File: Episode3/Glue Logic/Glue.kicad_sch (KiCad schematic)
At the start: 17 parts, among them U11 ATF22V10, U12 ATF750C, U7 ATF22V10C, U8 ATF22V10, U9 ATF750C, X1 1MHz

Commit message: Tied up a few loose ends in the PLD page.
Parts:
- X1: value 1MHz -> 20MHz
- renumbered R8 to R6, R6 to R8, U12 to U10

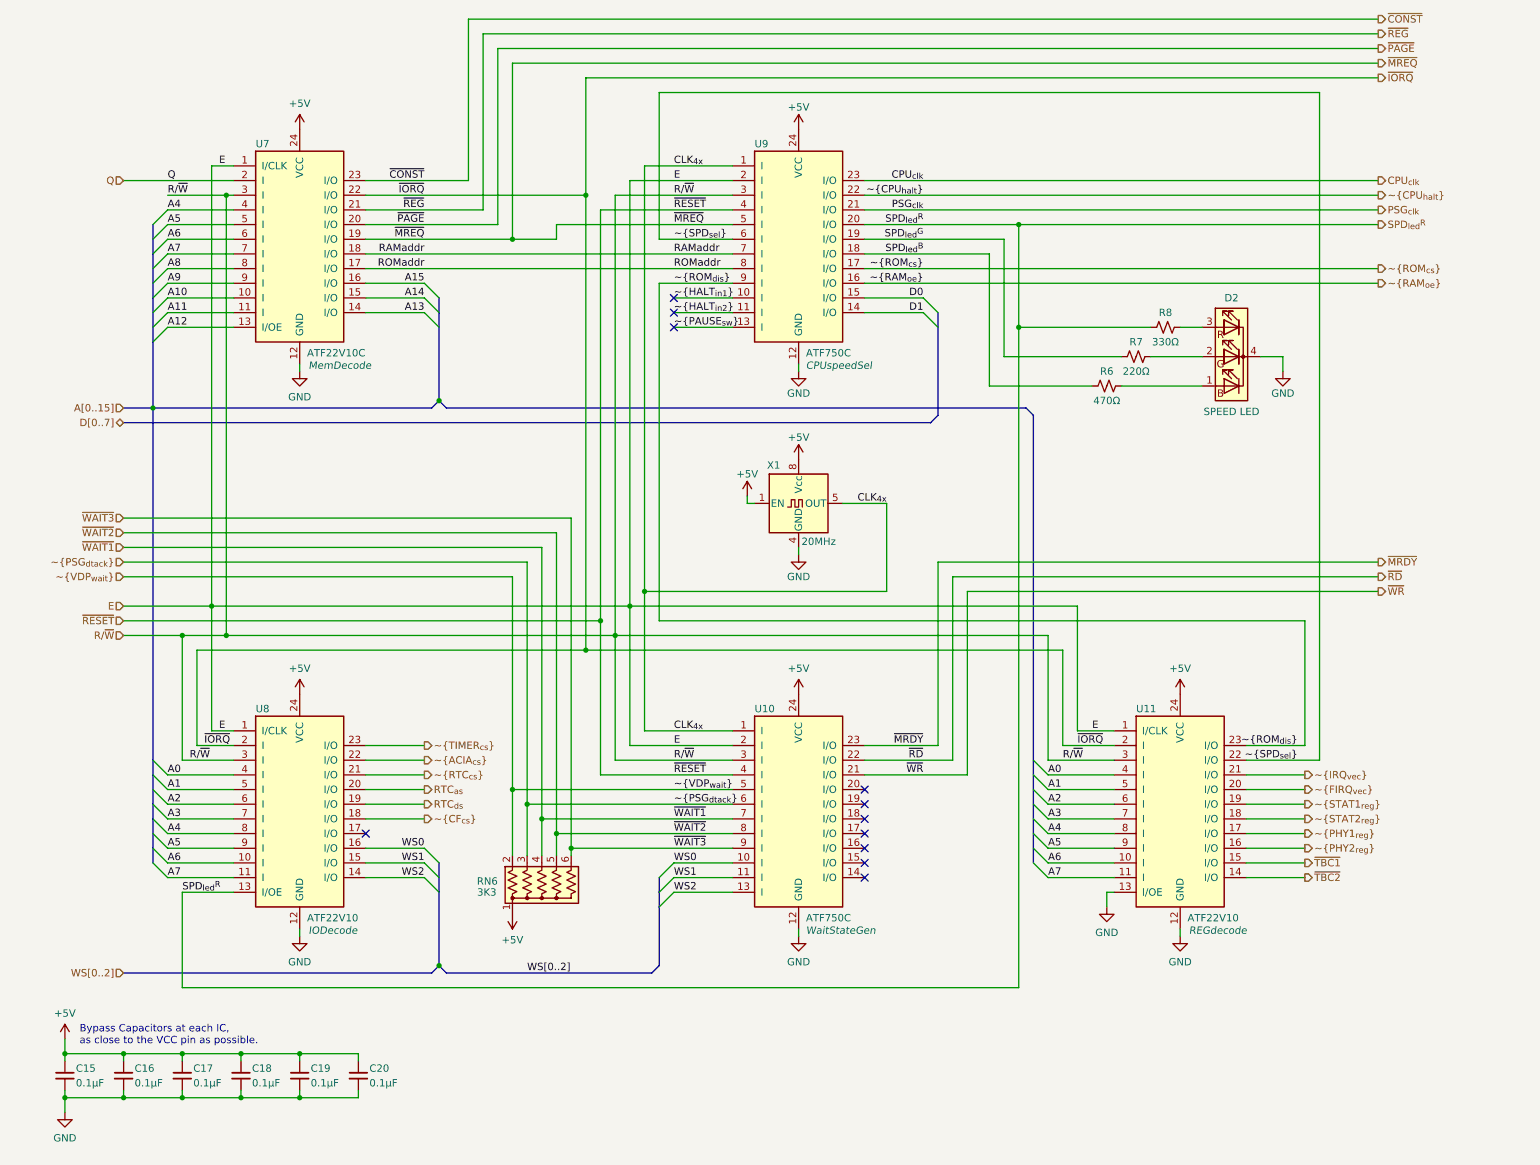
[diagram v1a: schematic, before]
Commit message: Corrected OE error
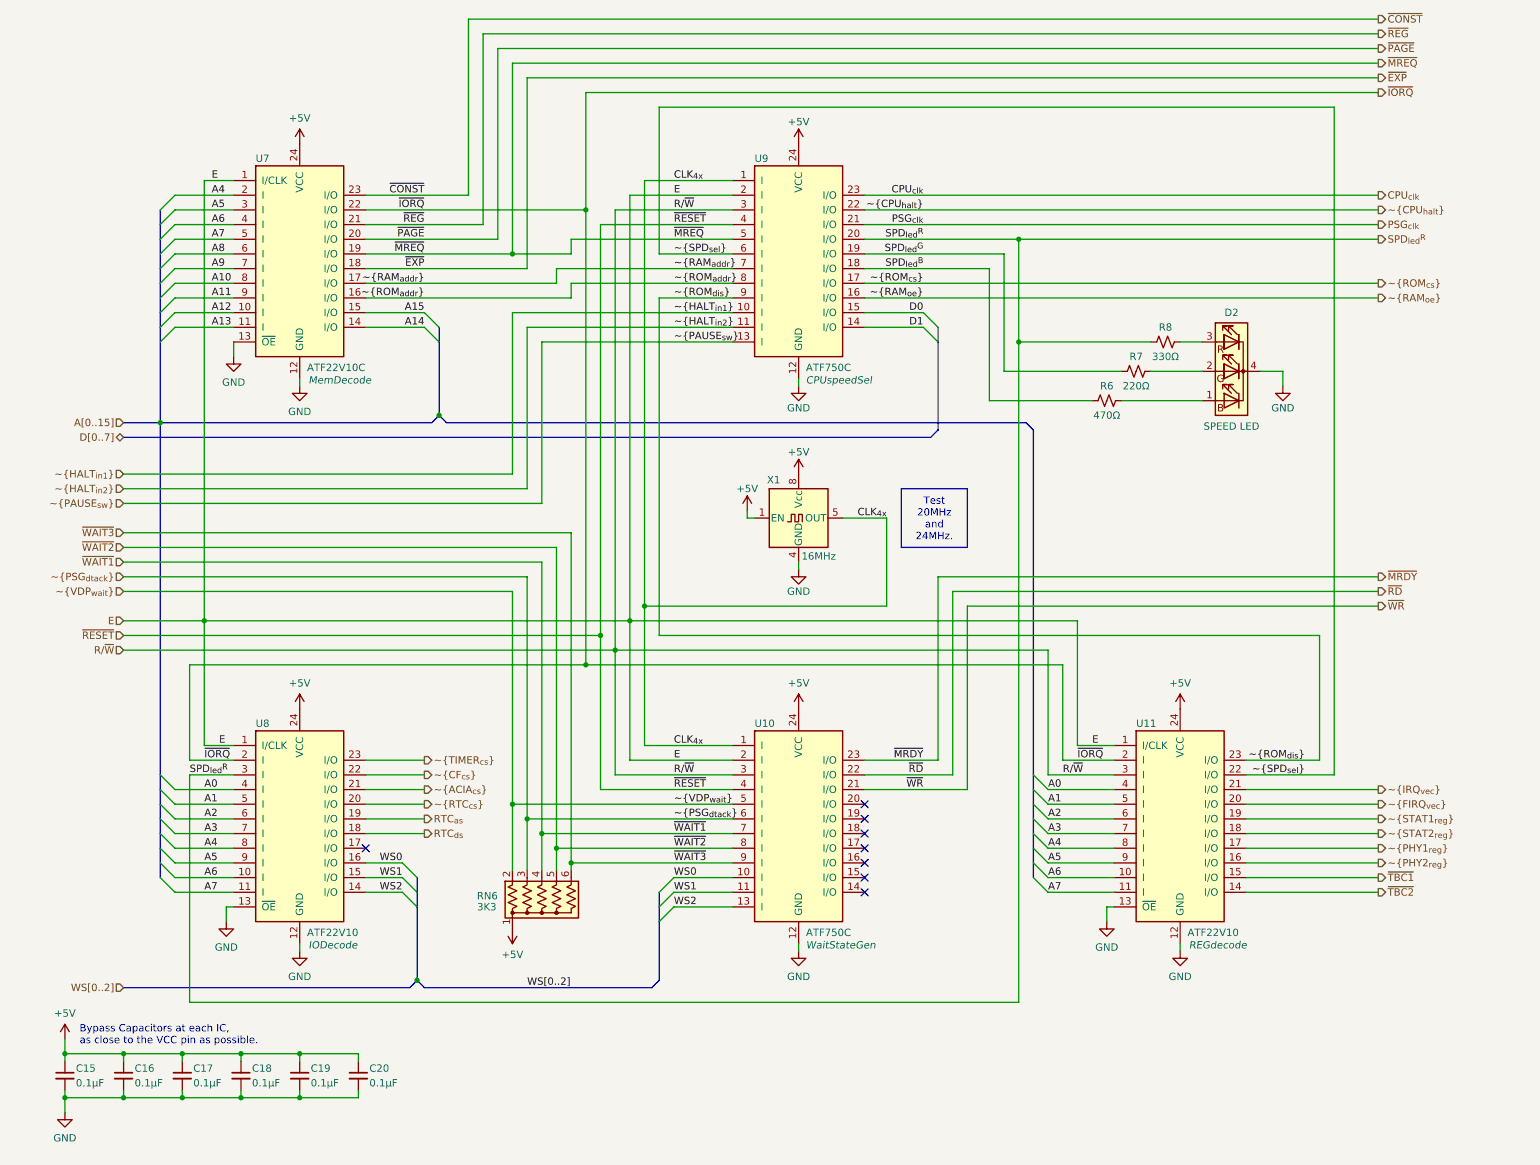
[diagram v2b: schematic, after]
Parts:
- X1: value 20MHz -> 16MHz
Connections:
- net Q is gone; now on net A4: U7.2 (I)
- net A10: now also U7.8 (I); no longer U7.10 (I)
- net A11: now also U7.9 (I); no longer U7.11 (I)
- net A12: now also U7.10 (I); no longer U7.13 (I/OE)
- net A13: now also U7.11 (I); no longer U7.14 (I/O)
- net A14: now also U7.14 (I/O); no longer U7.15 (I/O)
- net A15: now also U7.15 (I/O); no longer U7.16 (I/O)
- net A4: no longer U7.4 (I)
- net A5: now also U7.3 (I); no longer U7.5 (I)
- net A6: now also U7.4 (I); no longer U7.6 (I)
- net A7: now also U7.5 (I); no longer U7.7 (I)
- net A8: now also U7.6 (I); no longer U7.8 (I)
- net A9: now also U7.7 (I); no longer U7.9 (I)
- net GND: now also U7.13 (~{OE}), U8.13 (~{OE})
- net RTC_{as}: now also U8.19 (I/O); no longer U8.20 (I/O)
- net RTC_{ds}: now also U8.18 (I/O); no longer U8.19 (I/O)
- net R/~{W}: no longer U7.3 (I), U8.3 (I)
- net SPD_{led}^{R}: now also U8.3 (I); no longer U8.13 (I/OE)
- net ~{ACIA_{cs}}: now also U8.21 (I/O); no longer U8.22 (I/O)
- net ~{CF_{cs}}: now also U8.22 (I/O); no longer U8.18 (I/O)
- net ~{RTC_{cs}}: now also U8.20 (I/O); no longer U8.21 (I/O)
- net RAMaddr renamed ~{EXP}
- net ~{EXP}: no longer U9.7 (I)
- net ROMaddr renamed ~{RAM_{addr}}
- net ~{RAM_{addr}}: now also U9.7 (I); no longer U9.8 (I)
- new net ~{ROM_{addr}}: U7.16 (I/O), U9.8 (I)
- no-connect marks 11 -> 8
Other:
- moved on the sheet: D2, R6, R7, R8, RN6, U10, U11, U7, U8, U9, X1

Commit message: Major updates to PLDs
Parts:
- added R10, R13, R14, R15, R16, R17, R18, R9: 3K3Ω, symbol Device:R_Small_US
- RN6: value 3K3 -> 3K3Ω
- U10: Position (none) -> BB-Right
- U11: footprint Package_DIP:DIP-24_W7.62mm_Socket -> Package_DIP:DIP-24_W7.62mm_Socket_LongPads; Position (none) -> BB-C/Left
- U7: Position (none) -> BB-Left
- U8: footprint Package_DIP:DIP-24_W7.62mm_Socket -> Package_DIP:DIP-24_W7.62mm_Socket_LongPads; Position (none) -> BB-C/Right
- U9: Position (none) -> BB-Top
- X1: value 16MHz -> 12MHz
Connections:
- net PSG_{clk} is gone; now on net SPD_{led}^{R}: U9.21 (I/O)
- net ~{EXP} is gone; now on net ~{ROM_{addr}}: U7.18 (I/O)
- net ~{HALT_{in1}} is gone; now on net ~{ROM_{addr}}: U9.10 (I)
- net ~{HALT_{in2}} is gone; now on net ~{RAM_{addr}}: U9.11 (I)
- net ~{TBC1} is gone; now on net ~{RD}: U11.15 (I/O)
- net ~{TBC2} is gone; now on net ~{WR}: U11.14 (I/O)
- net +5V: now also R13.1, R15.1, R16.1, R17.1, R18.1
- net A0: now also U8.2 (I); no longer U8.4 (I)
- net A1: now also U8.3 (I); no longer U8.5 (I)
- net A14: now also U7.13 (I/OE); no longer U7.14 (I/O)
- net A15: now also U7.14 (I/O); no longer U7.15 (I/O)
- net A2: now also U8.4 (I); no longer U8.6 (I)
- net A3: now also U8.5 (I); no longer U8.7 (I)
- net A4: now also U8.6 (I); no longer U8.8 (I)
- net A5: now also U8.7 (I); no longer U8.9 (I)
- net A6: now also U8.8 (I); no longer U8.10 (I)
- net A7: now also U8.9 (I); no longer U8.11 (I)
- net CLK_{4x}: no longer U10.1 (I)
- net CPU_{clk}: now also U10.1 (I)
- net E: no longer U8.1 (I/CLK)
- net GND: now also U9.13 (I), R10.1, R14.1, R9.1; no longer U7.13 (~{OE}), U8.13 (~{OE})
- net SPD_{led}^{B}: now also U9.19 (I/O); no longer U9.18 (I/O)
- net SPD_{led}^{G}: now also U8.11 (I), U9.20 (I/O); no longer U9.19 (I/O)
- net SPD_{led}^{R}: now also U8.10 (I); no longer U8.3 (I), U9.20 (I/O)
- net WS0: now also R14.2
- net WS1: now also R9.2
- net WS2: now also R10.2; no longer U8.14 (I/O)
- net ~{IORQ}: now also U8.1 (I/CLK); no longer U8.2 (I)
- net ~{PAUSE_{sw}}: now also U9.9 (I), R17.2; no longer U9.13 (I)
- net ~{RAM_{addr}}: now also R16.2; no longer U9.7 (I)
- net ~{RD}: no longer U10.22 (I/O)
- net ~{ROM_{addr}}: now also R15.2; no longer U7.16 (I/O), U9.8 (I)
- net ~{ROM_{dis}}: now also U9.6 (I); no longer U9.9 (I)
- net ~{SPD_{sel}}: now also U9.7 (I); no longer U9.6 (I)
- net ~{WR}: no longer U10.21 (I/O)
- net ~{USB_{cs}}: now reaches U8.17 (I/O)
- new net: R13.2, U8.13 (I/OE), U8.14 (I/O)
- new net ~{HALT_{in}}: R18.2, U9.8 (I)
- new net ~{RAM_{cs}}*: U9.18 (I/O)
- no-connect marks 8 -> 11
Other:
- moved on the sheet: C15, C16, C17, C18, C19, C20, D2, R6, R7, R8, RN6, U10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

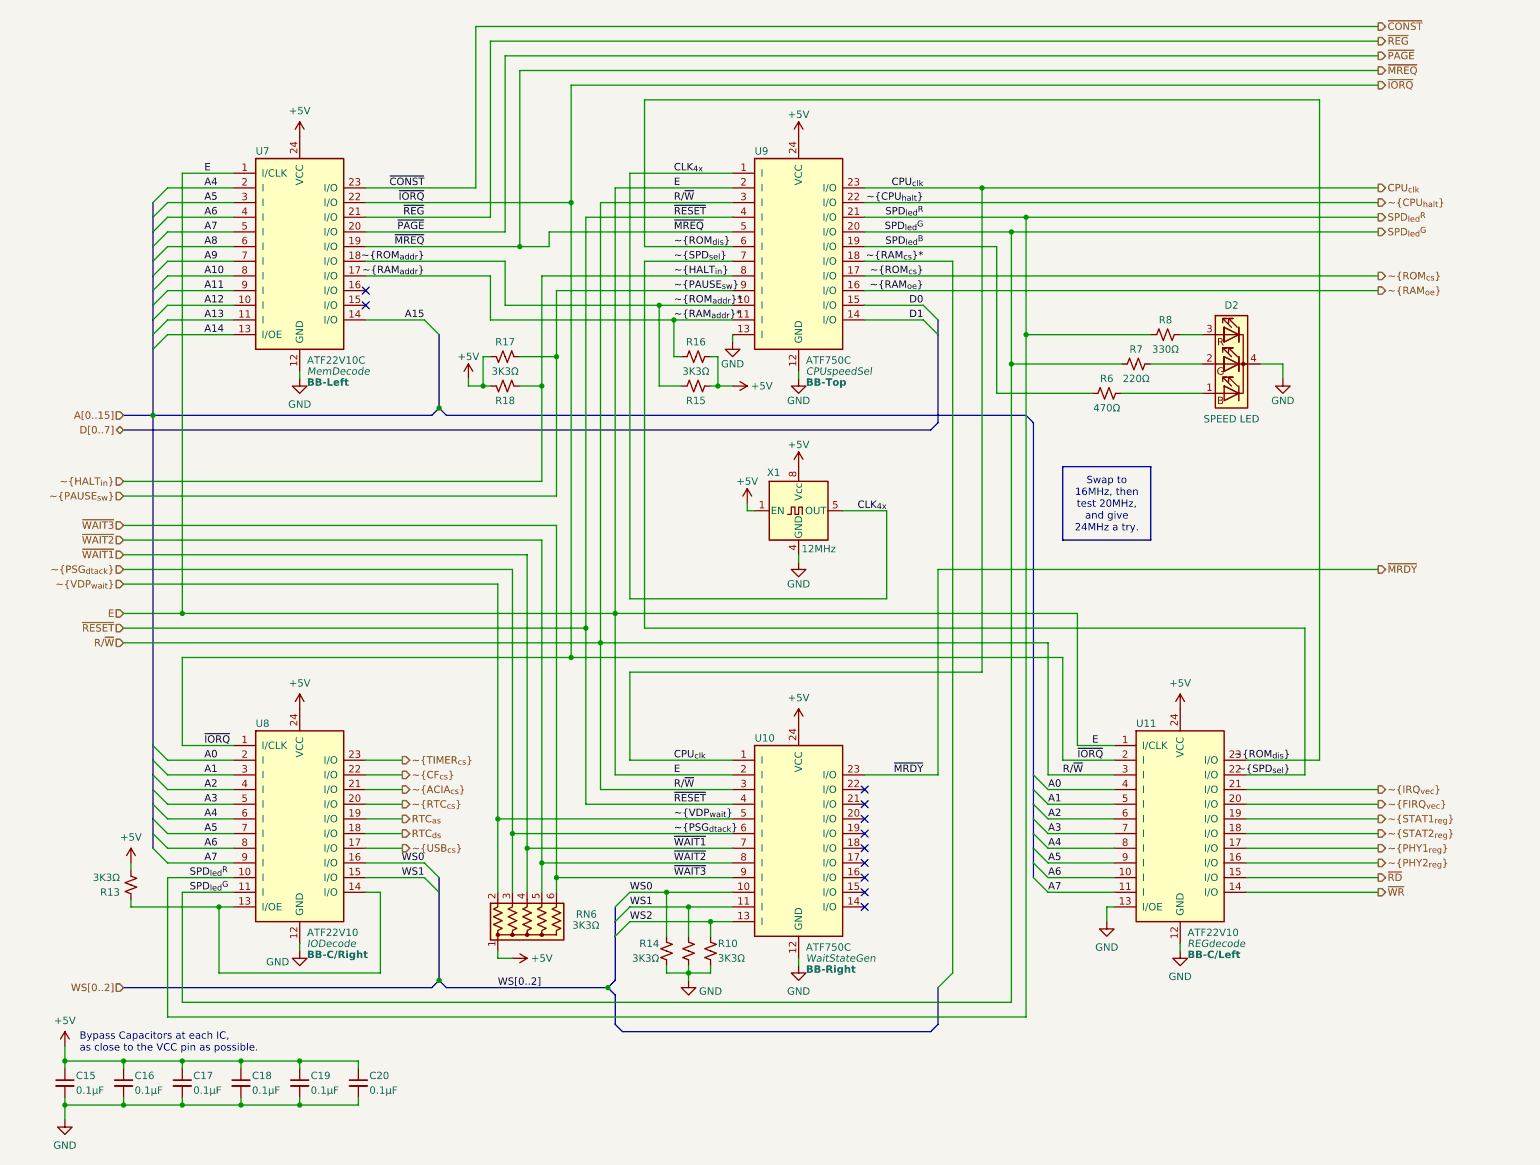
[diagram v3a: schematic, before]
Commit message: Reduced PLDs from 5 to 4, and optimized macrocells to the maximum
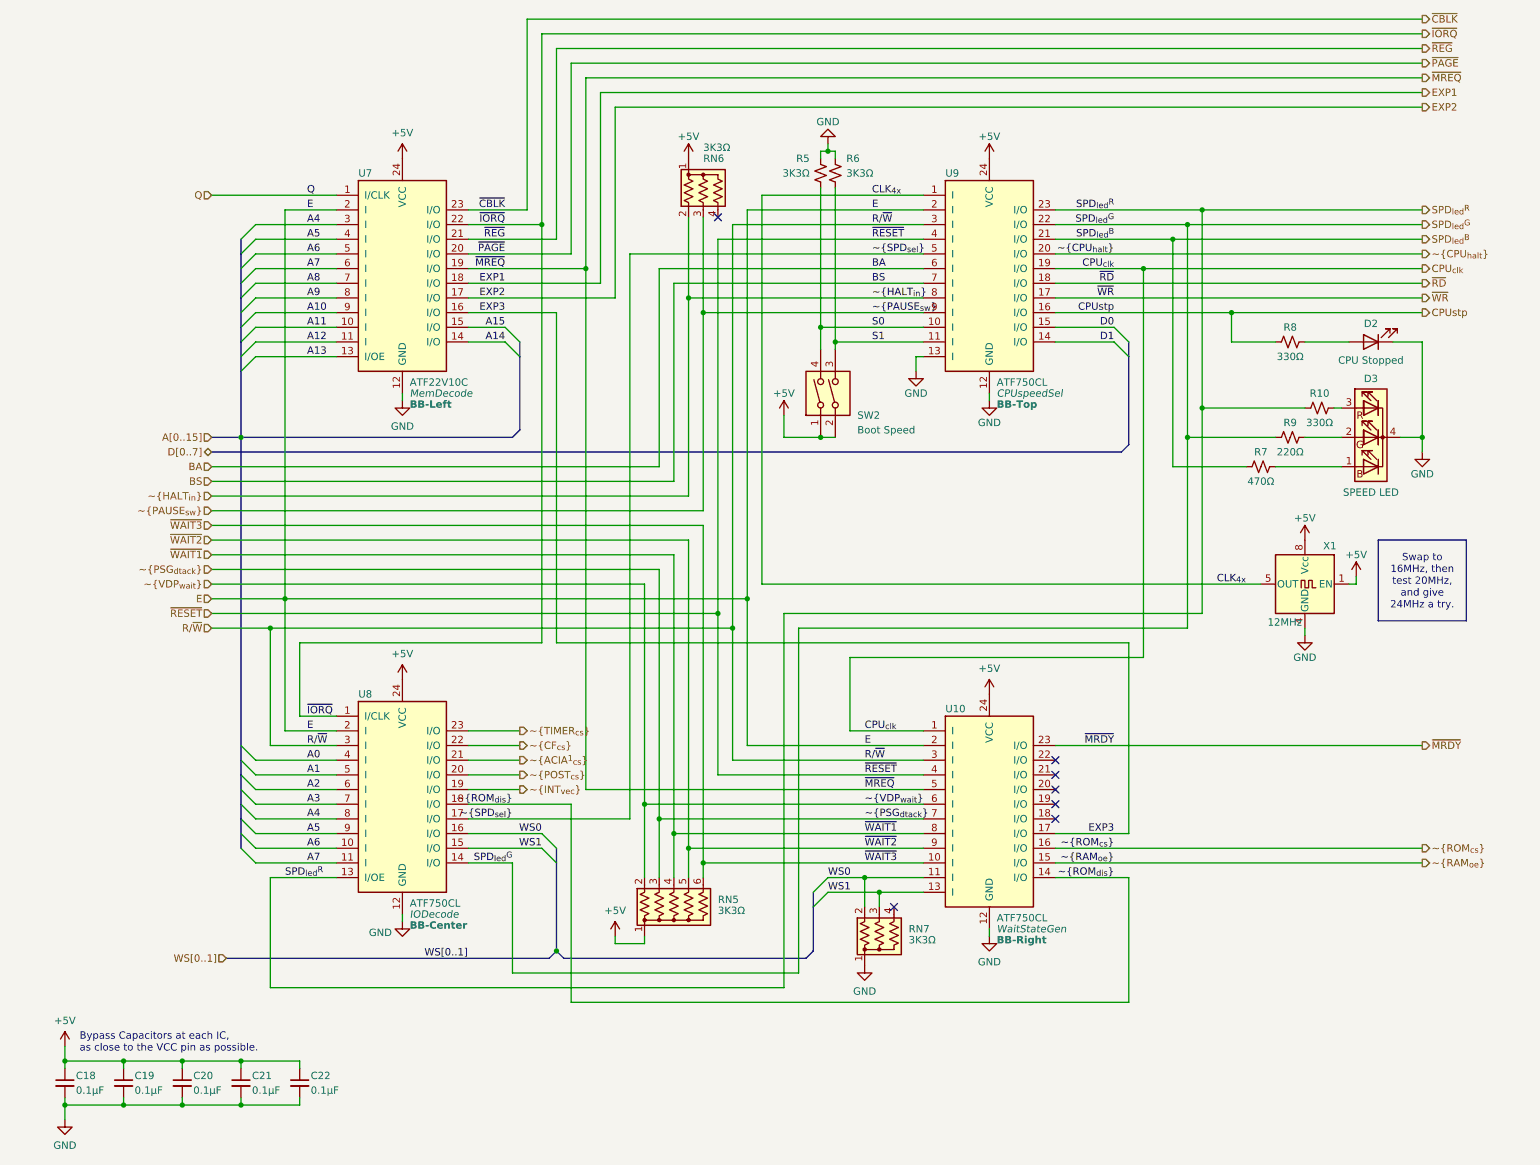
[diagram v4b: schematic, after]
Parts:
- removed C20: 0.1µF, symbol Device:C_Small
- removed R10, R13, R14, R15, R16, R17, R18, R9: 3K3Ω, symbol Device:R_Small_US
- removed U11: ATF22V10, Package_DIP:DIP-24_W7.62mm_Socket_LongPads, symbol MicroHobbyist:ATF22V10C
- added D2: CPU Stopped, symbol Device:LED
- added R5, R6: 3K3Ω, symbol Device:R_Small_US
- added R8: 330Ω, symbol Device:R_Small_US
- added RN6, RN7: 3K3Ω, Resistor_THT:R_Array_SIP4, symbol Device:R_Network03_US
- added SW2: Boot Speed, symbol Switch:SW_DIP_x02
- U10, U9: value ATF750C -> ATF750CL
- U8: value ATF22V10 -> ATF750CL; Position BB-C/Right -> BB-Center
- renumbered C15 to C18, C16 to C19, C17 to C20, C18 to C21, C19 to C22, D2 to D3, R8 to R10, R6 to R7, R7 to R9, RN6 to RN5
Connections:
- net RTC_{ds} is gone; now on net ~{ROM_{dis}}: U8.18 (I/O)
- net WS2 is gone; now on net WS1: U10.13 (I)
- net ~{RAM_{cs}}* is gone; now on net ~{RD}: U9.18 (I/O)
- net ~{USB_{cs}} is gone; now on net ~{SPD_{sel}}: U8.17 (I/O)
- net +5V: now also RN6.1 (common), SW2.1, SW2.2
- net A0: now also U8.4 (I); no longer U8.2 (I)
- net A1: now also U8.5 (I); no longer U8.3 (I)
- net A10: now also U7.9 (I); no longer U7.8 (I)
- net A11: now also U7.10 (I); no longer U7.9 (I)
- net A12: now also U7.11 (I); no longer U7.10 (I)
- net A13: now also U7.13 (I/OE); no longer U7.11 (I)
- net A14: now also U7.14 (I/O); no longer U7.13 (I/OE)
- net A15: now also U7.15 (I/O); no longer U7.14 (I/O)
- net A2: now also U8.6 (I); no longer U8.4 (I)
- net A3: now also U8.7 (I); no longer U8.5 (I)
- net A4: now also U7.3 (I), U8.8 (I); no longer U7.2 (I), U8.6 (I)
- net A5: now also U7.4 (I), U8.9 (I); no longer U7.3 (I), U8.7 (I)
- net A6: now also U7.5 (I), U8.10 (I); no longer U7.4 (I), U8.8 (I)
- net A7: now also U7.6 (I), U8.11 (I); no longer U7.5 (I), U8.9 (I)
- net A8: now also U7.7 (I); no longer U7.6 (I)
- net A9: now also U7.8 (I); no longer U7.7 (I)
- net CPU_{clk}: now also U9.19 (I/O); no longer U9.23 (I/O)
- net E: now also U7.2 (I), U8.2 (I); no longer U7.1 (I/CLK)
- net GND: now also D2.1 (K), R5.2, R6.2, RN7.1 (common)
- net R/~{W}: now also U8.3 (I)
- net SPD_{led}^{B}: now also U9.21 (I/O); no longer U9.19 (I/O)
- net SPD_{led}^{G}: now also U8.14 (I/O), U9.22 (I/O); no longer U8.11 (I), U9.20 (I/O)
- net SPD_{led}^{R}: now also U8.13 (I/OE), U9.23 (I/O); no longer U8.10 (I), U9.21 (I/O)
- net WS0: now also U10.11 (I), RN7.2 (R1); no longer U10.10 (I)
- net WS1: now also RN7.3 (R2); no longer U10.11 (I)
- net ~{CPU_{halt}}: now also U9.20 (I/O); no longer U9.22 (I/O)
- net ~{HALT_{in}}: now also RN6.2 (R1)
- net ~{MREQ}: now also U10.5 (I); no longer U9.5 (I)
- net ~{PAUSE_{sw}}: now also RN6.3 (R2)
- net ~{PSG_{dtack}}: now also U10.7 (I); no longer U10.6 (I)
- net ~{RAM_{oe}}: now also U10.15 (I/O); no longer U9.16 (I/O)
- net ~{ROM_{cs}}: now also U10.16 (I/O); no longer U9.17 (I/O)
- net ~{ROM_{dis}}: now also U10.14 (I/O); no longer U9.6 (I)
- net ~{SPD_{sel}}: now also U9.5 (I); no longer U9.7 (I)
- net ~{VDP_{wait}}: now also U10.6 (I); no longer U10.5 (I)
- net ~{WAIT1}: now also U10.8 (I); no longer U10.7 (I)
- net ~{WAIT2}: now also U10.9 (I); no longer U10.8 (I)
- net ~{WAIT3}: now also U10.10 (I); no longer U10.9 (I)
- net ~{WR}: now also U9.17 (I/O)
- net EXP3: now reaches U10.17 (I/O)
- net EXP3: now also U7.16 (I/O)
- net RTC_{as} renamed ~{INT_{vec}}
- net ~{ACIA_{cs}} renamed ~{ACIA^{1}_{cs}}
- net ~{CONST} renamed ~{CBLK}
- net ~{RAM_{addr}} renamed EXP2
- net EXP2: no longer U9.11 (I)
- net ~{ROM_{addr}} renamed EXP1
- net EXP1: no longer U9.10 (I)
- net ~{RTC_{cs}} renamed ~{POST_{cs}}
- new net: D2.2 (A), R8.2
- new net BA: U9.6 (I)
- new net BS: U9.7 (I)
- new net CPUstp: R8.1, U9.16 (I/O)
- new net Q: U7.1 (I/CLK)
- new net S0: R5.1, SW2.4, U9.10 (I)
- new net S1: R6.1, SW2.3, U9.11 (I)
- no-connect marks 11 -> 7
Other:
- moved on the sheet: D3, R10, R7, R9, RN5, U10, U7, U8, U9, X1
